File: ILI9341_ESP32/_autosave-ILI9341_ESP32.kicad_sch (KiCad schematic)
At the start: 46 parts, among them J1 USB_C_Receptacle_USB2.0_16P, J10 Conn_01x01_Pin, J9 Conn_01x01_Pin, Q1 BC817, Q4 BC817, SW1 SS-12F23-G040, U1 HE6250xx, U10 CH340K, U2 XM5062S, U7 02FVS3

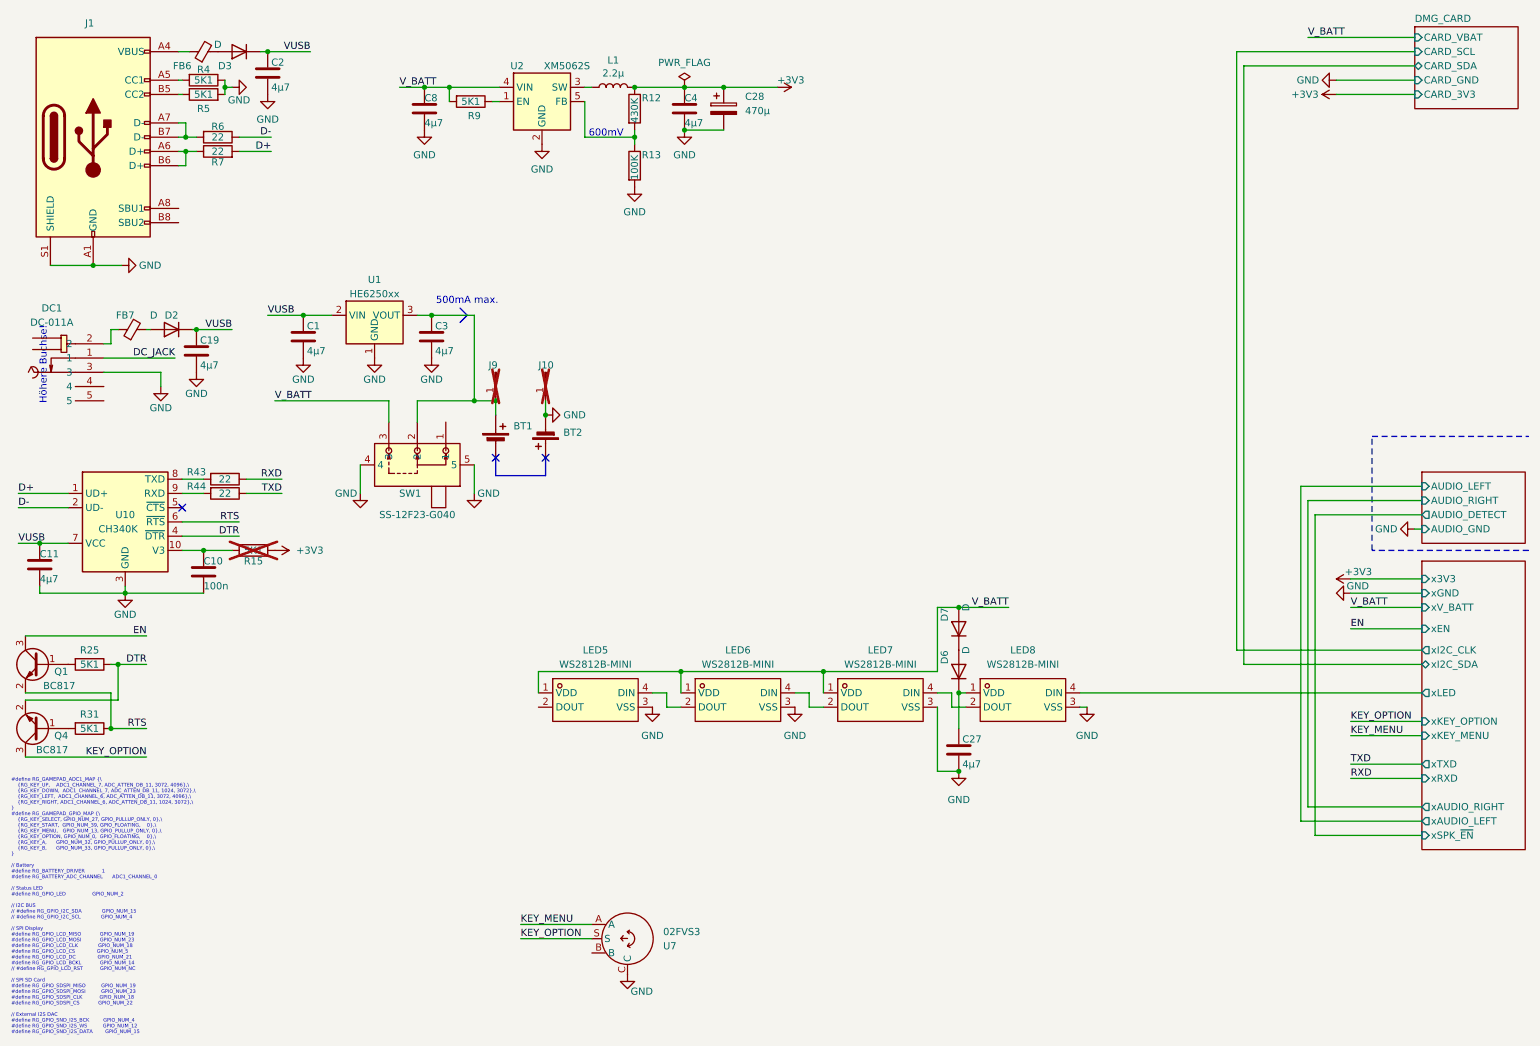
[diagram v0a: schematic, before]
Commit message: update nimh charger and battery protection
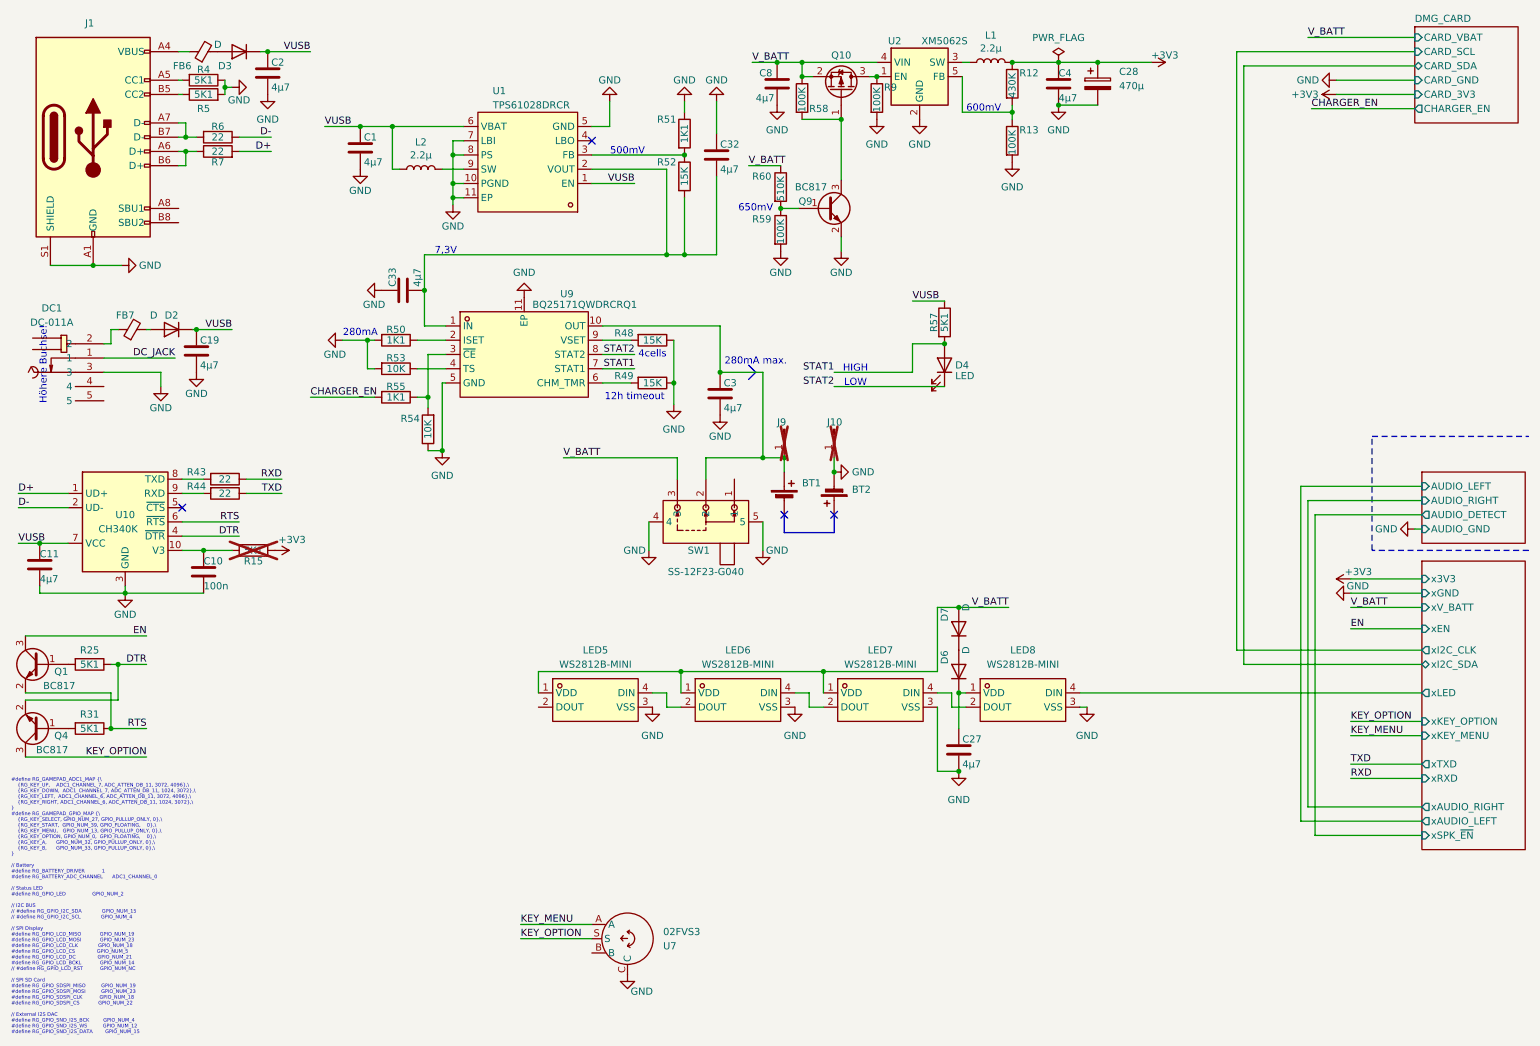
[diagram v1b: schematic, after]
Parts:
- removed U1: HE6250xx, Package_TO_SOT_SMD:SOT-89-3, symbol Regulator_Linear:HT75xx-1-SOT89
- added C32, C33: 4µ7, Capacitor_SMD:C_1206_3216Metric, symbol Device:C
- added D4: LED, LED_SMD:LED_0603_1608Metric, symbol Device:LED
- added L2: 2.2µ, Inductor_SMD:L_1210_3225Metric_Pad1.42x2.65mm_HandSolder, symbol Device:L
- added Q10: Q_PMOS_GSD, Package_TO_SOT_SMD:SOT-323_SC-70, symbol Device:Q_PMOS_GSD
- added Q9: BC817, Package_TO_SOT_SMD:SOT-323_SC-70, symbol Transistor_BJT:BC817
- added R48, R49, R52: 15K, Resistor_SMD:R_0603_1608Metric, symbol Device:R
- added R50, R51, R55: 1K1, Resistor_SMD:R_0603_1608Metric, symbol Device:R
- added R53, R54: 10K, Resistor_SMD:R_0603_1608Metric, symbol Device:R
- added R57: 5K1, Resistor_SMD:R_0603_1608Metric, symbol Device:R
- added R58, R59: 100K, Resistor_SMD:R_0603_1608Metric, symbol Device:R
- added R60: 510K, Resistor_SMD:R_0603_1608Metric, symbol Device:R
- added U1: TPS61028DRCR, easyeda2kicad:VSON-10_L3.0-W3.0-P0.50-TL-EP-1, symbol easyeda2kicad:TPS61028DRCR
- added U9: BQ25171QWDRCRQ1, easyeda2kicad:VSON-10_L3.0-W3.0-P0.50-BL-EP1.65, symbol easyeda2kicad:BQ25171QWDRCRQ1
- R12, R13, R15, R25, R31, R4, R43, R44, R5, R6, R7: footprint Resistor_SMD:R_0603_1608Metric_Pad0.98x0.95mm_HandSolder -> Resistor_SMD:R_0603_1608Metric
- R9: value 5K1 -> 100K; footprint Resistor_SMD:R_0603_1608Metric_Pad0.98x0.95mm_HandSolder -> Resistor_SMD:R_0603_1608Metric; LCSC C26000 -> C15458
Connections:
- net GND: now also R9.2, C32.1, C33.1, Q9.2 (E), R48.1, R49.1, R50.2, R51.1, R53.2, R54.1, R59.2, U1.10 (PGND), U1.11 (EP), U1.5 (GND), U1.7 (LBI), U1.8 (PS), U9.11 (EP), U9.5 (GND)
- net VUSB: now also L2.1, R57.1, U1.1 (EN), U1.6 (VBAT)
- net V_BATT: now also Q10.2 (S), R58.1, R60.1; no longer R9.2
- net at BT1.1 (+), C3.1, J9.1 (Pin_1)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: now also U9.10 (OUT)
- net at R9.1, U2.1 (EN): now also Q10.3 (D)
- new net: R54.2, R55.1, U9.3 (~{CE})
- new net: C32.2, C33.2, R52.2, U1.2 (VOUT), U9.1 (IN)
- new net: R51.2, R52.1, U1.3 (FB)
- new net: L2.2, U1.9 (SW)
- new net: Q9.1 (B), R59.1, R60.2
- new net: Q10.1 (G), Q9.3 (C), R58.2
- new net: R50.1, U9.2 (ISET)
- new net: R53.1, U9.4 (TS)
- new net: R49.2, U9.6 (CHM_TMR)
- new net: R48.2, U9.9 (VSET)
- new net CHARGER_EN: R55.2
- new net STAT1: D4.2 (A), R57.2, U9.7 (STAT1)
- new net STAT2: D4.1 (K), U9.8 (STAT2)
- no-connect marks 3 -> 4
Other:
- sheet DMG_CARD ports: added CHARGER_EN; removed none
- note added: "12h timeout"
- note added: "280mA"
- note added: "280mA max."
- note added: "4cells"
- note added: "500mV"
- note added: "650mV"
- note added: "7,3V"
- note added: "HIGH"
- note added: "LOW"
- note removed: "500mA max."
- moved on the sheet: BT1, BT2, C1, C28, C3, C4, C8, J10, J9, L1, R12, R13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
